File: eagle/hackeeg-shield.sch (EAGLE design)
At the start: 141 parts, among them IC1 ADS1299IPAG, IC10 TXB0108PWR, IC11 TXB0108PWR, IC2 TPS72325DBVT, IC3 TPS73225DBVT, IC5 24AA256UID, IC6 TPS60403DBVT, IC7 OPA376DBV, IC8 OPA376DBV, IC9 TXS0102DCUR

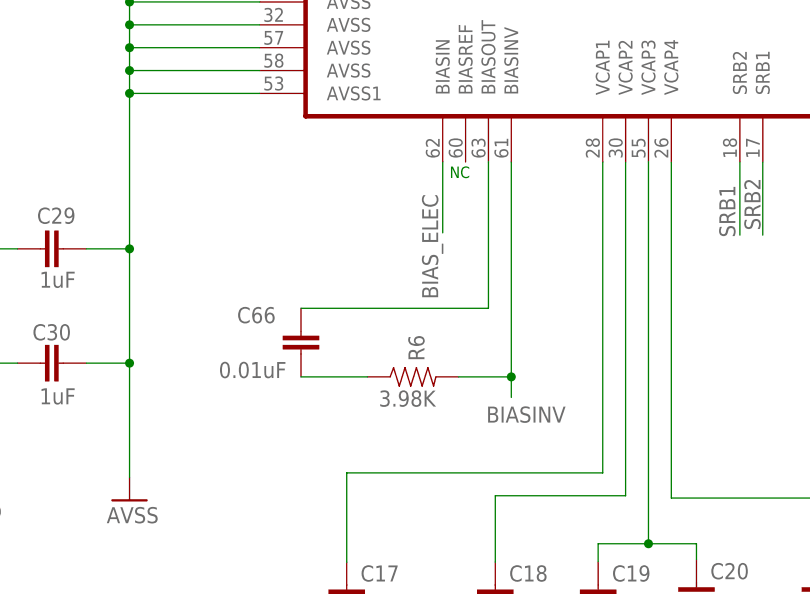
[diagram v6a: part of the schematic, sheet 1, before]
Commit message: fixed problem with BIASOUT/BIASINV
- for common mode noise rejection
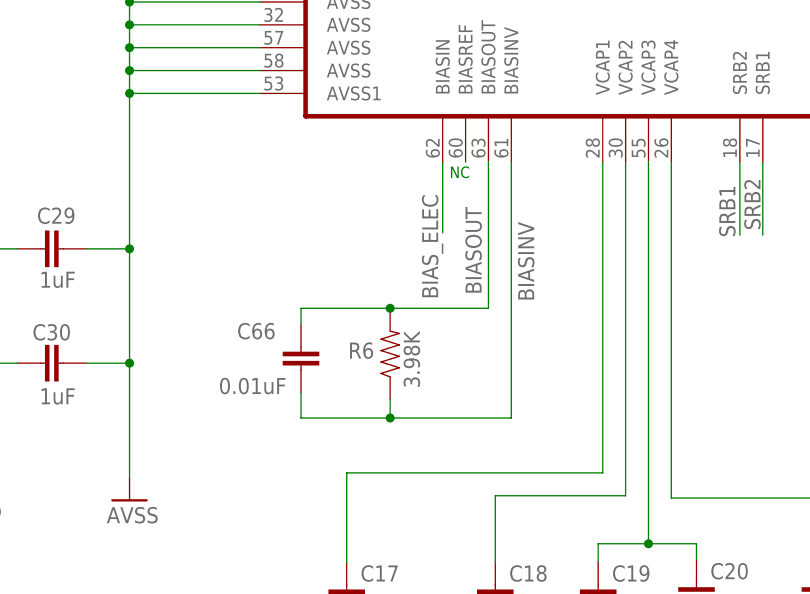
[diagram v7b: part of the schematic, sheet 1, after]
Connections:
- removed net N$22: C66.2, R6.1
- removed net N$25: C66.1, IC1.BIASOUT
- new net BIASOUT: C66.1, IC1.BIASOUT, R6.2
- net BIASINV: now also C66.2, R6.1; no longer R6.2
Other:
- moved on the sheet: C66, R6
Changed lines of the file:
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@@
 <grid distance="0.1" unitdist="inch" unit="inch" style="lines" multiple="1" display="no" altdistance="0.01" altunitdist="inch" altunit="inch"/>
 <layers>
-<layer number="1" name="Top" color="4" fill="1" visible="yes" active="no"/>
-<layer number="2" name="Route2" color="3" fill="1" visible="yes" active="no"/>
-<layer number="3" name="Route3" color="4" fill="3" visible="yes" active="no"/>
-<layer number="14" name="Route14" color="1" fill="6" visible="yes" active="no"/>
-<layer number="15" name="Route15" color="15" fill="1" visible="yes" active="no"/>
-<layer number="16" name="Bottom" color="1" fill="1" visible="yes" active="no"/>
-<layer number="17" name="Pads" color="2" fill="1" visible="yes" active="no"/>
-<layer number="18" name="Vias" color="2" fill="1" visible="yes" active="no"/>
-<layer number="19" name="Unrouted" color="14" fill="1" visible="yes" active="no"/>
-<layer number="20" name="Dimension" color="15" fill="1" visible="yes" active="no"/>
-<layer number="21" name="tPlace" color="7" fill="1" visible="yes" active="no"/>
-<layer number="22" name="bPlace" color="7" fill="1" visible="yes" active="no"/>
-<layer number="23" name="tOrigins" color="15" fill="1" visible="yes" active="no"/>
-<layer number="24" name="bOrigins" color="15" fill="1" visible="yes" active="no"/>
-<layer number="25" name="tNames" color="7" fill="1" visible="yes" active="no"/>
-<layer number="26" name="bNames" color="7" fill="1" visible="yes" active="no"/>
-<layer number="27" name="tValues" color="7" fill="1" visible="yes" active="no"/>
-<layer number="28" name="bValues" color="7" fill="1" visible="yes" active="no"/>
+<layer number="1" name="Top" color="4" fill="1" visible="no" active="no"/>
+<layer number="2" name="Route2" color="3" fill="1" visible="no" active="no"/>
+<layer number="3" name="Route3" color="4" fill="3" visible="no" active="no"/>
+<layer number="14" name="Route14" color="1" fill="6" visible="no" active="no"/>
+<layer number="15" name="Route15" color="15" fill="1" visible="no" active="no"/>
+<layer number="16" name="Bottom" color="1" fill="1" visible="no" active="no"/>
+<layer number="17" name="Pads" color="2" fill="1" visible="no" active="no"/>
+<layer number="18" name="Vias" color="2" fill="1" visible="no" active="no"/>
+<layer number="19" name="Unrouted" color="14" fill="1" visible="no" active="no"/>
+<layer number="20" name="Dimension" color="15" fill="1" visible="no" active="no"/>
+<layer number="21" name="tPlace" color="7" fill="1" visible="no" active="no"/>
+<layer number="22" name="bPlace" color="7" fill="1" visible="no" active="no"/>
+<layer number="23" name="tOrigins" color="15" fill="1" visible="no" active="no"/>
+<layer number="24" name="bOrigins" color="15" fill="1" visible="no" active="no"/>
+<layer number="25" name="tNames" color="7" fill="1" visible="no" active="no"/>
+<layer number="26" name="bNames" color="7" fill="1" visible="no" active="no"/>
+<layer number="27" name="tValues" color="7" fill="1" visible="no" active="no"/>
+<layer number="28" name="bValues" color="7" fill="1" visible="no" active="no"/>
 <layer number="29" name="tStop" color="3" fill="9" visible="no" active="no"/>
 <layer number="30" name="bStop" color="7" fill="6" visible="no" active="no"/>
@@
 <layer number="35" name="tGlue" color="7" fill="4" visible="no" active="no"/>
 <layer number="36" name="bGlue" color="7" fill="5" visible="no" active="no"/>
-<layer number="37" name="tTest" color="7" fill="1" visible="yes" active="no"/>
-<layer number="38" name="bTest" color="7" fill="1" visible="yes" active="no"/>
+<layer number="37" name="tTest" color="7" fill="1" visible="no" active="no"/>
+<layer number="38" name="bTest" color="7" fill="1" visible="no" active="no"/>
 <layer number="39" name="tKeepout" color="13" fill="1" visible="no" active="no"/>
 <layer number="40" name="bKeepout" color="5" fill="1" visible="no" active="no"/>
@@
 <layer number="44" name="Drills" color="7" fill="1" visible="no" active="no"/>
 <layer number="45" name="Holes" color="7" fill="1" visible="no" active="no"/>
-<layer number="46" name="Milling" color="3" fill="1" visible="yes" active="no"/>
-<layer number="47" name="Measures" color="7" fill="1" visible="yes" active="no"/>
-<layer number="48" name="Document" color="7" fill="1" visible="yes" active="no"/>
-<layer number="49" name="Reference" color="7" fill="1" visible="yes" active="no"/>
-<layer number="50" name="dxf" color="7" fill="1" visible="yes" active="no"/>
-<layer number="51" name="tDocu" color="6" fill="1" visible="yes" active="no"/>
-<layer number="52" name="bDocu" color="6" fill="1" visible="yes" active="no"/>
-<layer number="53" name="tGND_GNDA" color="7" fill="9" visible="yes" active="no"/>
-<layer number="54" name="bGND_GNDA" color="1" fill="9" visible="yes" active="no"/>
-<layer number="56" name="wert" color="7" fill="1" visible="yes" active="no"/>
-<layer number="57" name="tCAD" color="7" fill="1" visible="yes" active="no"/>
+<layer number="46" name="Milling" color="3" fill="1" visible="no" active="no"/>
+<layer number="47" name="Measures" color="7" fill="1" visible="no" active="no"/>
+<layer number="48" name="Document" color="7" fill="1" visible="no" active="no"/>
+<layer number="49" name="Reference" color="7" fill="1" visible="no" active="no"/>
+<layer number="50" name="dxf" color="7" fill="1" visible="no" active="no"/>
+<layer number="51" name="tDocu" color="6" fill="1" visible="no" active="no"/>
+<layer number="52" name="bDocu" color="6" fill="1" visible="no" active="no"/>
+<layer number="53" name="tGND_GNDA" color="7" fill="9" visible="no" active="no"/>
+<layer number="54" name="bGND_GNDA" color="1" fill="9" visible="no" active="no"/>
+<layer number="56" name="wert" color="7" fill="1" visible="no" active="no"/>
+<layer number="57" name="tCAD" color="7" fill="1" visible="no" active="no"/>
 <layer number="91" name="Nets" color="2" fill="1" visible="yes" active="yes"/>
 <layer number="92" name="Busses" color="1" fill="1" visible="yes" active="yes"/>
@@
 <attribute name="VALUE" x="310.388" y="81.534" size="1.778" layer="96"/>
 </instance>
-<instance part="C66" gate="G$1" x="255.27" y="122.936" smashed="yes">
-<attribute name="NAME" x="248.158" y="126.365" size="1.778" layer="95"/>
-<attribute name="VALUE" x="246.126" y="120.269" size="1.778" layer="96"/>
-</instance>
-<instance part="R6" gate="G$1" x="267.716" y="120.396" smashed="yes">
-<attribute name="NAME" x="268.986" y="122.1486" size="1.778" layer="95" rot="R90"/>
-<attribute name="VALUE" x="263.906" y="117.094" size="1.778" layer="96"/>
+<instance part="C66" gate="G$1" x="255.27" y="121.158" smashed="yes">
+<attribute name="NAME" x="248.158" y="124.587" size="1.778" layer="95"/>
+<attribute name="VALUE" x="246.126" y="118.491" size="1.778" layer="96"/>
+</instance>
+<instance part="R6" gate="G$1" x="265.176" y="122.936" smashed="yes" rot="R90">
+<attribute name="NAME" x="263.4234" y="124.206" size="1.778" layer="95" rot="R180"/>
+<attribute name="VALUE" x="268.478" y="119.126" size="1.778" layer="96" rot="R90"/>
 </instance>
 <instance part="SUPPLY16" gate="G$1" x="63.754" y="73.406"/>
@@
 <segment>
 <pinref part="IC1" gate="G$1" pin="BIASINV"/>
-<pinref part="R6" gate="G$1" pin="2"/>
-<wire x1="278.638" y1="144.272" x2="278.638" y2="120.396" width="0.1524" layer="91"/>
-<wire x1="278.638" y1="120.396" x2="272.796" y2="120.396" width="0.1524" layer="91"/>
-<wire x1="278.638" y1="120.396" x2="278.638" y2="118.11" width="0.1524" layer="91"/>
-<junction x="278.638" y="120.396"/>
-<label x="275.844" y="115.316" size="1.778" layer="95"/>
-</segment>
-</net>
-<net name="N$22" class="0">
-<segment>
+<wire x1="278.638" y1="144.272" x2="278.638" y2="115.824" width="0.1524" layer="91"/>
+<pinref part="C66" gate="G$1" pin="2"/>
+<wire x1="255.27" y1="118.618" x2="255.27" y2="115.824" width="0.1524" layer="91"/>
+<wire x1="255.27" y1="115.824" x2="265.176" y2="115.824" width="0.1524" layer="91"/>
 <pinref part="R6" gate="G$1" pin="1"/>
-<wire x1="262.636" y1="120.396" x2="255.27" y2="120.396" width="0.1524" layer="91"/>
-<pinref part="C66" gate="G$1" pin="2"/>
-</segment>
-</net>
-<net name="N$25" class="0">
+<wire x1="265.176" y1="115.824" x2="278.638" y2="115.824" width="0.1524" layer="91"/>
+<wire x1="265.176" y1="117.856" x2="265.176" y2="115.824" width="0.1524" layer="91"/>
+<junction x="265.176" y="115.824"/>
+<label x="281.178" y="128.778" size="1.778" layer="95" rot="R90"/>
+</segment>
+</net>
+<net name="BIASOUT" class="0">
 <segment>
 <pinref part="C66" gate="G$1" pin="1"/>
 <pinref part="IC1" gate="G$1" pin="BIASOUT"/>
-<wire x1="255.27" y1="128.016" x2="276.098" y2="128.016" width="0.1524" layer="91"/>
+<wire x1="255.27" y1="126.238" x2="255.27" y2="128.016" width="0.1524" layer="91"/>
+<wire x1="255.27" y1="128.016" x2="265.176" y2="128.016" width="0.1524" layer="91"/>
+<wire x1="265.176" y1="128.016" x2="276.098" y2="128.016" width="0.1524" layer="91"/>
 <wire x1="276.098" y1="128.016" x2="276.098" y2="144.272" width="0.1524" layer="91"/>
-</segment>
-</net>
+<pinref part="R6" gate="G$1" pin="2"/>
+<junction x="265.176" y="128.016"/>
+<label x="275.336" y="129.54" size="1.778" layer="95" rot="R90"/>
+</segment>
+</net>

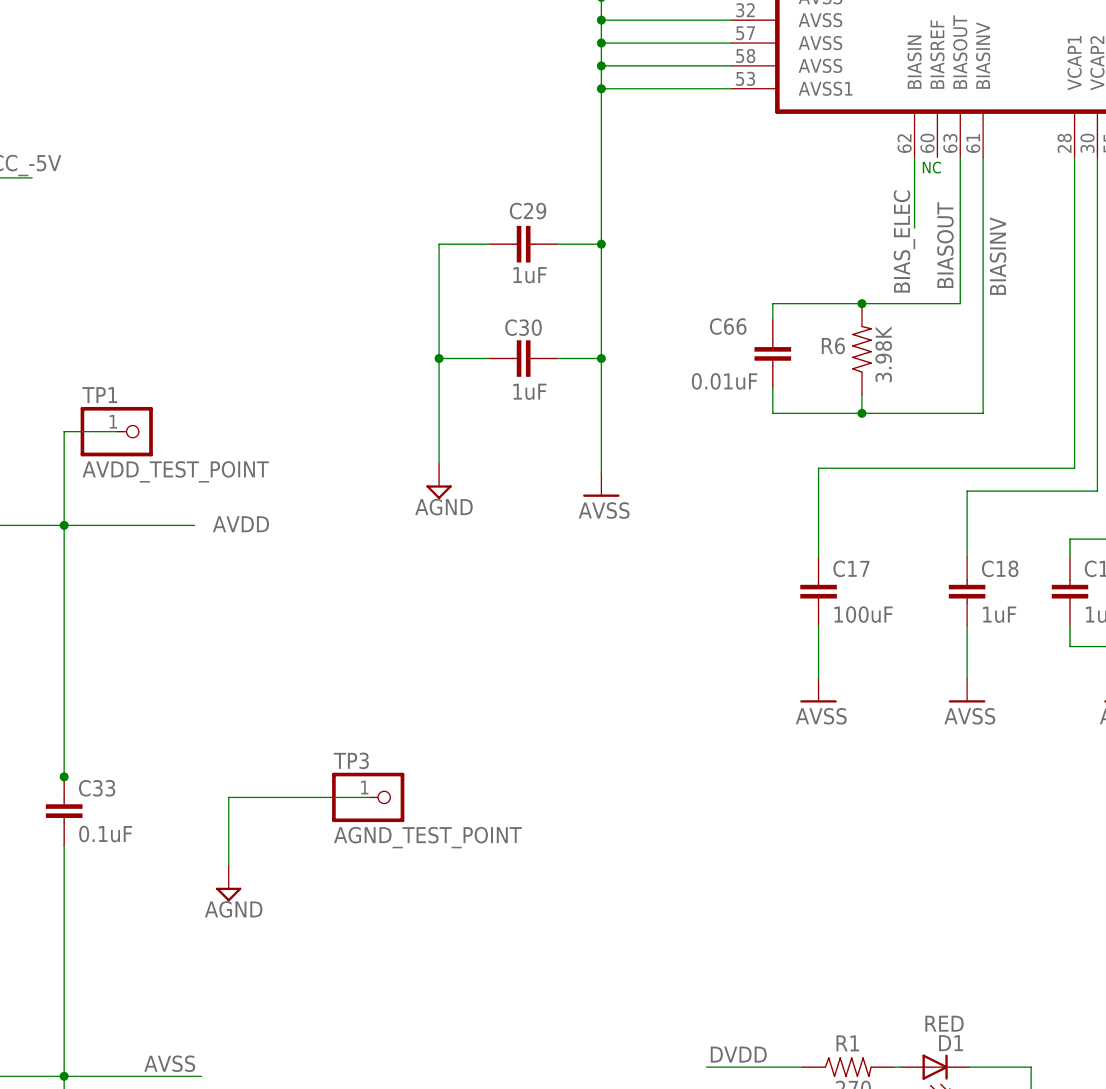
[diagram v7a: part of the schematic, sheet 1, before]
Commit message: added JP9 - BIASIN/BIAS_ELEC/BIASOUT config
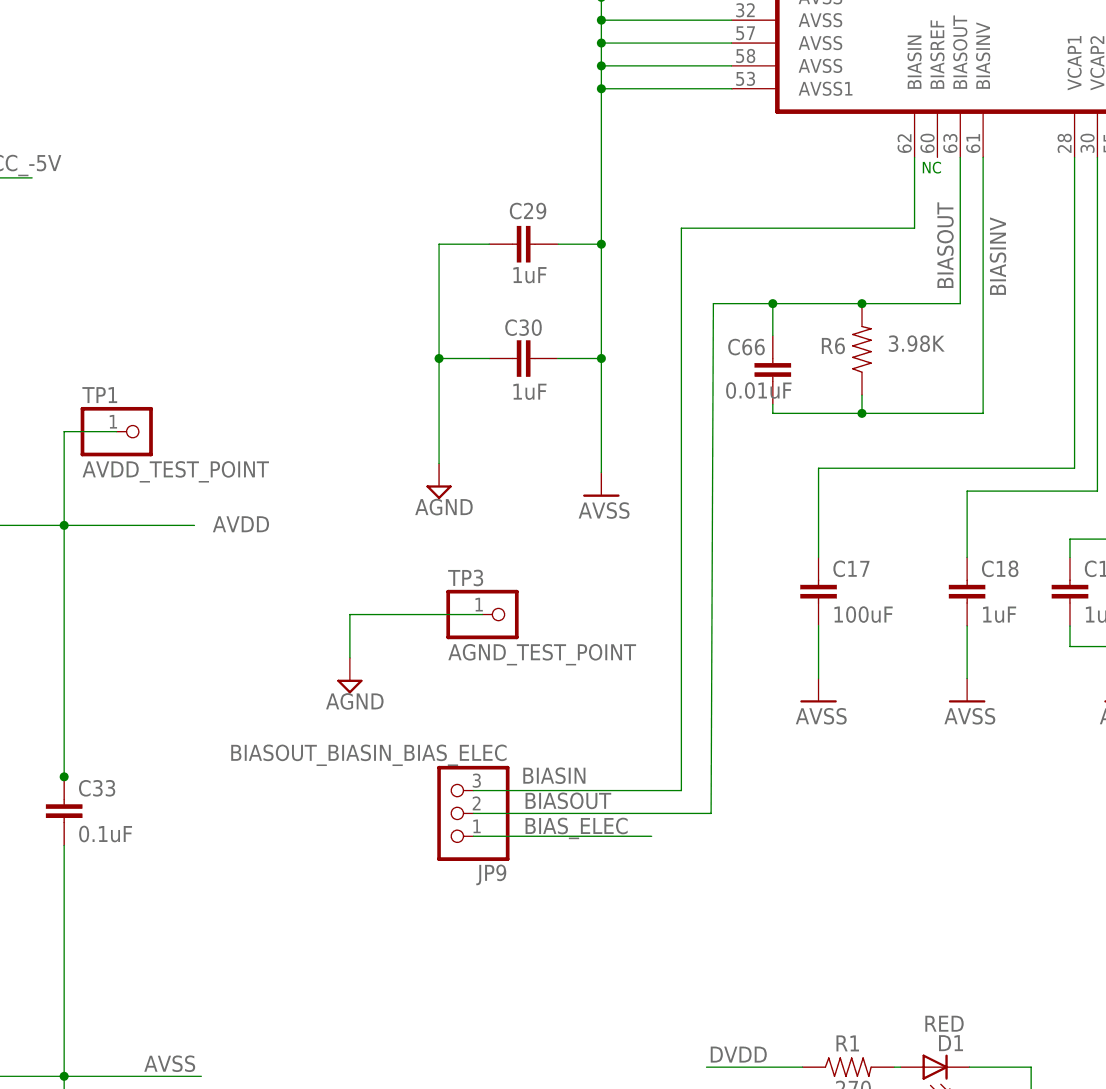
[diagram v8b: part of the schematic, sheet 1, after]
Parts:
- added JP9: BIASOUT_BIASIN_BIAS_ELEC, headers:PINHD-1X3
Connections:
- new net BIASIN: IC1.BIASIN, JP9.3
- net BIASOUT: now also JP9.2
- net BIAS_ELEC: now also JP9.1; no longer IC1.BIASIN
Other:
- moved on the sheet: C66, TP3
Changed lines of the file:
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@@
 <part name="IC7" library="OPA376" deviceset="OPA376" device="DBV"/>
 <part name="TP4" library="adafruit" deviceset="PINHD-1X1" device="" value="VREFP_TEST_POINT"/>
+<part name="JP9" library="headers" deviceset="PINHD-1X3" device="" value="BIASOUT_BIASIN_BIAS_ELEC"/>
 </parts>
 <sheets>
@@
 <instance part="D1" gate="G$1" x="272.034" y="43.18" rot="R90"/>
 <instance part="TP1" gate="G$1" x="184.912" y="113.792"/>
-<instance part="TP3" gate="G$1" x="212.852" y="73.152"/>
-<instance part="SUPPLY55" gate="G$1" x="194.818" y="62.992"/>
+<instance part="TP3" gate="G$1" x="225.552" y="93.472"/>
+<instance part="SUPPLY55" gate="G$1" x="208.28" y="86.106"/>
 <instance part="TP2" gate="G$1" x="188.214" y="33.782"/>
 <instance part="C25" gate="G$1" x="112.522" y="222.504"/>
@@
 <attribute name="VALUE" x="310.388" y="81.534" size="1.778" layer="96"/>
 </instance>
-<instance part="C66" gate="G$1" x="255.27" y="121.158" smashed="yes">
-<attribute name="NAME" x="248.158" y="124.587" size="1.778" layer="95"/>
-<attribute name="VALUE" x="246.126" y="118.491" size="1.778" layer="96"/>
+<instance part="C66" gate="G$1" x="255.27" y="119.38" smashed="yes">
+<attribute name="NAME" x="250.19" y="122.301" size="1.778" layer="95"/>
+<attribute name="VALUE" x="249.936" y="117.475" size="1.778" layer="96"/>
 </instance>
 <instance part="R6" gate="G$1" x="265.176" y="122.936" smashed="yes" rot="R90">
 <attribute name="NAME" x="263.4234" y="124.206" size="1.778" layer="95" rot="R180"/>
-<attribute name="VALUE" x="268.478" y="119.126" size="1.778" layer="96" rot="R90"/>
+<attribute name="VALUE" x="274.32" y="124.46" size="1.778" layer="96" rot="R180"/>
 </instance>
 <instance part="SUPPLY16" gate="G$1" x="63.754" y="73.406"/>
@@
 <attribute name="VALUE" x="297.688" y="266.446" size="1.778" layer="96" rot="MR0"/>
 </instance>
+<instance part="JP9" gate="A" x="219.456" y="71.374" rot="R180"/>
 </instances>
 <busses>
@@
 </segment>
 </net>
-<net name="BIAS_ELEC" class="0">
-<segment>
-<wire x1="271.018" y1="144.272" x2="271.018" y2="136.398" width="0.1524" layer="91"/>
-<label x="270.51" y="129.032" size="1.778" layer="95" rot="R90"/>
-<pinref part="IC1" gate="G$1" pin="BIASIN"/>
-</segment>
-</net>
 <net name="CLK" class="0">
 <segment>
@@
 <segment>
 <pinref part="TP3" gate="G$1" pin="1"/>
-<wire x1="210.312" y1="73.152" x2="194.818" y2="73.152" width="0.1524" layer="91"/>
-<wire x1="194.818" y1="73.152" x2="194.818" y2="65.532" width="0.1524" layer="91"/>
+<wire x1="223.012" y1="93.472" x2="208.28" y2="93.472" width="0.1524" layer="91"/>
+<wire x1="208.28" y1="93.472" x2="208.28" y2="88.646" width="0.1524" layer="91"/>
 <pinref part="SUPPLY55" gate="G$1" pin="AGND"/>
 </segment>
@@
 <wire x1="278.638" y1="144.272" x2="278.638" y2="115.824" width="0.1524" layer="91"/>
 <pinref part="C66" gate="G$1" pin="2"/>
-<wire x1="255.27" y1="118.618" x2="255.27" y2="115.824" width="0.1524" layer="91"/>
+<wire x1="255.27" y1="116.84" x2="255.27" y2="115.824" width="0.1524" layer="91"/>
 <wire x1="255.27" y1="115.824" x2="265.176" y2="115.824" width="0.1524" layer="91"/>
 <pinref part="R6" gate="G$1" pin="1"/>
@@
 <pinref part="C66" gate="G$1" pin="1"/>
 <pinref part="IC1" gate="G$1" pin="BIASOUT"/>
-<wire x1="255.27" y1="126.238" x2="255.27" y2="128.016" width="0.1524" layer="91"/>
+<wire x1="255.27" y1="124.46" x2="255.27" y2="128.016" width="0.1524" layer="91"/>
 <wire x1="255.27" y1="128.016" x2="265.176" y2="128.016" width="0.1524" layer="91"/>
 <wire x1="265.176" y1="128.016" x2="276.098" y2="128.016" width="0.1524" layer="91"/>
@@
 <junction x="265.176" y="128.016"/>
 <label x="275.336" y="129.54" size="1.778" layer="95" rot="R90"/>
+<wire x1="255.27" y1="128.016" x2="248.666" y2="128.016" width="0.1524" layer="91"/>
+<wire x1="248.666" y1="128.016" x2="248.412" y2="71.374" width="0.1524" layer="91"/>
+<wire x1="248.412" y1="71.374" x2="221.996" y2="71.374" width="0.1524" layer="91"/>
+<pinref part="JP9" gate="A" pin="2"/>
+<label x="227.584" y="71.882" size="1.778" layer="95"/>
+<junction x="255.27" y="128.016"/>
 </segment>
 </net>
@@
 </segment>
 </net>
+<net name="BIASIN" class="0">
+<segment>
+<wire x1="271.018" y1="144.272" x2="271.018" y2="136.398" width="0.1524" layer="91"/>
+<pinref part="IC1" gate="G$1" pin="BIASIN"/>
+<wire x1="271.018" y1="136.398" x2="245.11" y2="136.398" width="0.1524" layer="91"/>
+<wire x1="245.11" y1="136.398" x2="245.11" y2="73.914" width="0.1524" layer="91"/>
+<pinref part="JP9" gate="A" pin="3"/>
+<wire x1="221.996" y1="73.914" x2="245.11" y2="73.914" width="0.1524" layer="91"/>
+<label x="227.33" y="74.676" size="1.778" layer="95"/>
+</segment>
+</net>
+<net name="BIAS_ELEC" class="0">
+<segment>
+<pinref part="JP9" gate="A" pin="1"/>
+<wire x1="221.996" y1="68.834" x2="241.808" y2="68.834" width="0.1524" layer="91"/>
+<label x="227.584" y="69.088" size="1.778" layer="95"/>
+</segment>
+</net>
